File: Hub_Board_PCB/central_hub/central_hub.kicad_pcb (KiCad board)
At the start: 2 copper layers, 0.6 x 1.7 mm, 90 parts, among them J1 CAN_OUT, J10 Conn_02x03_Counter_Clockwise, J2 Barrel_Jack_MountingPin, J3 Screw_Terminal_01x14, J4 Conn_02x05_Counter_Clockwise, J5 CSP-USC16-TR, J6 Screw_Terminal_01x08, J7 Conn_02x03_Counter_Clockwise, J8 Conn_01x02, J9 Screw_Terminal_01x04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

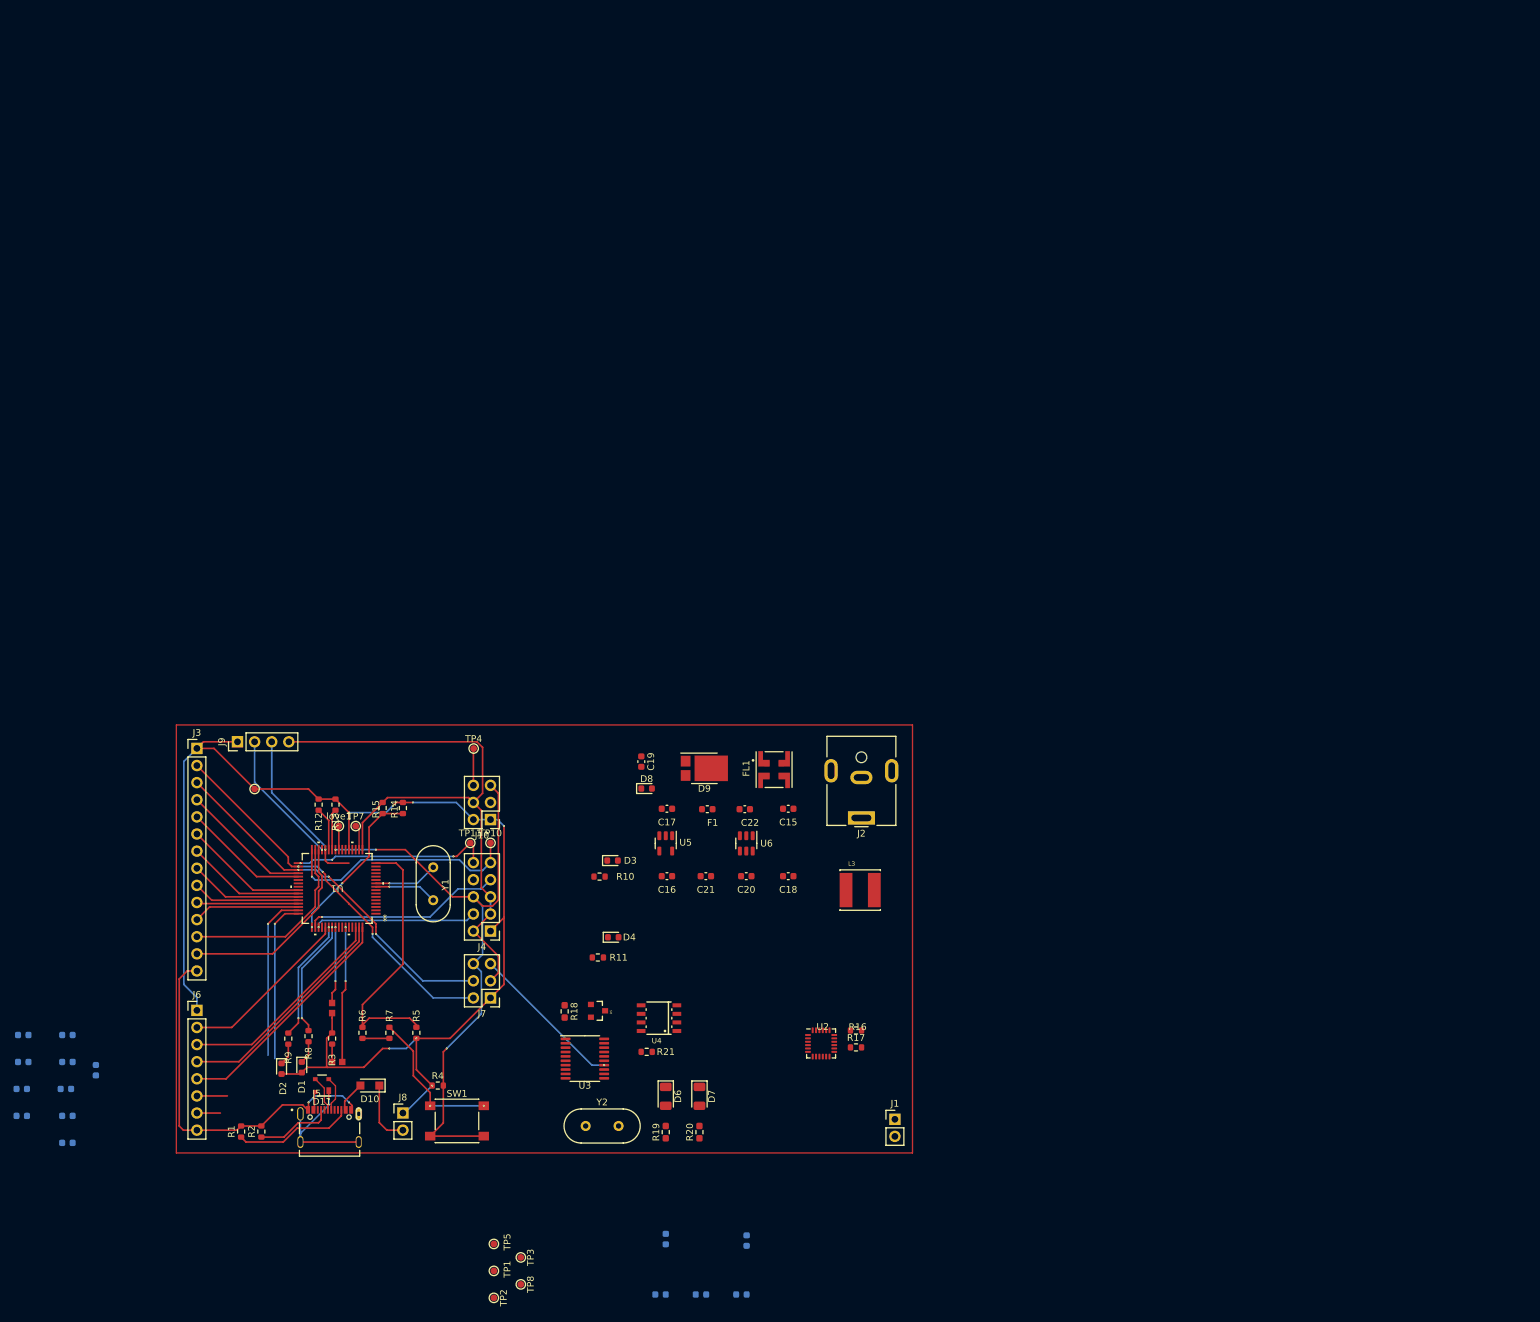
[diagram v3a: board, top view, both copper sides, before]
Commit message: Added new connectors as per brandons new shifters
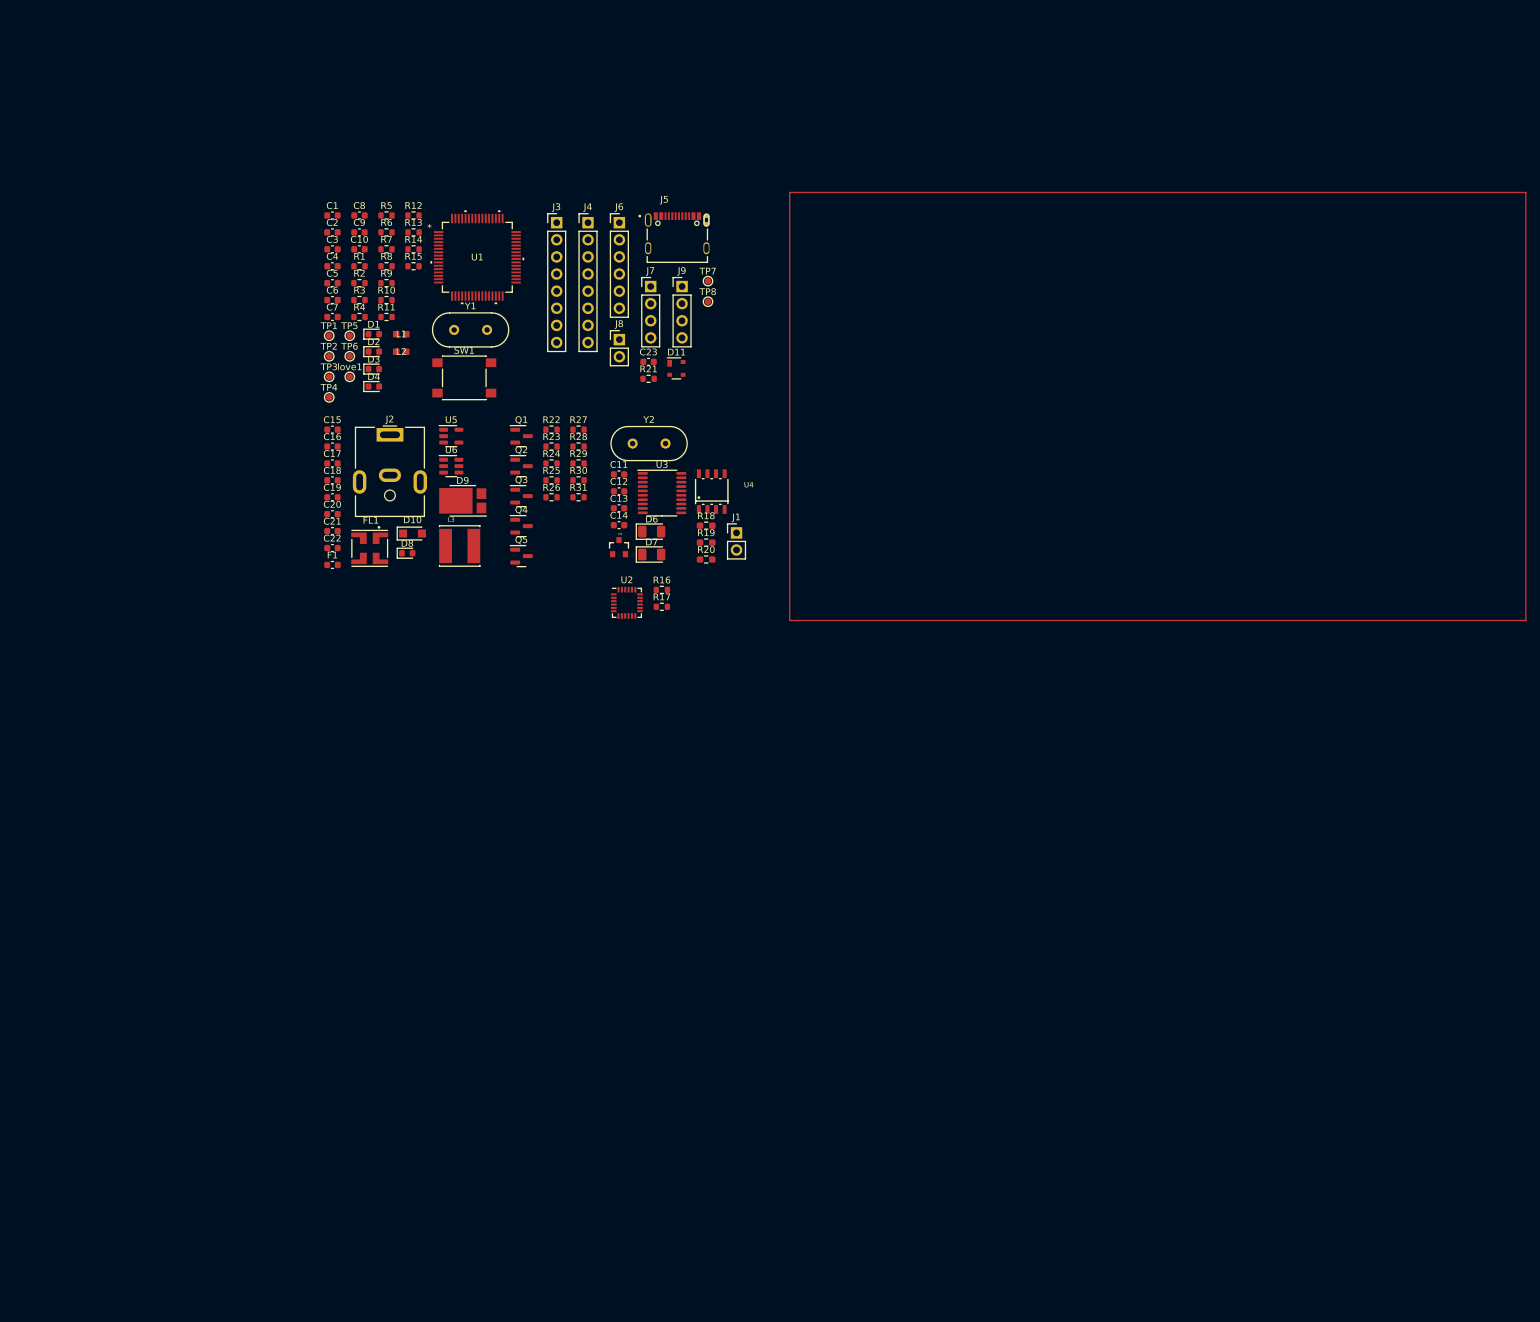
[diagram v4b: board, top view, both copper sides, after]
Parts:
- removed J10: Conn_02x03_Counter_Clockwise, Connector_PinHeader_2.54mm:PinHeader_2x03_P2.54mm_Vertical
- removed TP10, TP11: TestPoint, TestPoint:TestPoint_Pad_D1.0mm
- added Q1: BSS138, Package_TO_SOT_SMD:SOT-23, F.Cu at (139.6, 31.6)
- added Q2: BSS138, Package_TO_SOT_SMD:SOT-23, F.Cu at (139.6, 36.1)
- added Q3: BSS138, Package_TO_SOT_SMD:SOT-23, F.Cu at (139.6, 40.5)
- added Q4: BSS138, Package_TO_SOT_SMD:SOT-23, F.Cu at (139.6, 45.0)
- added Q5: BSS138, Package_TO_SOT_SMD:SOT-23, F.Cu at (139.6, 49.5)
- added R22: 10k, Resistor_SMD:R_0603_1608Metric, F.Cu at (144.1, 30.7)
- added R23: 10k, Resistor_SMD:R_0603_1608Metric, F.Cu at (144.1, 33.2)
- added R24: 10k, Resistor_SMD:R_0603_1608Metric, F.Cu at (144.1, 35.7)
- added R25: 10k, Resistor_SMD:R_0603_1608Metric, F.Cu at (144.1, 38.2)
- added R26: 10k, Resistor_SMD:R_0603_1608Metric, F.Cu at (144.1, 40.7)
- added R27: 10k, Resistor_SMD:R_0603_1608Metric, F.Cu at (148.1, 30.7)
- added R28: 10k, Resistor_SMD:R_0603_1608Metric, F.Cu at (148.1, 33.2)
- added R29: 10k, Resistor_SMD:R_0603_1608Metric, F.Cu at (148.1, 35.7)
- added R30: 10k, Resistor_SMD:R_0603_1608Metric, F.Cu at (148.1, 38.2)
- added R31: 10k, Resistor_SMD:R_0603_1608Metric, F.Cu at (148.1, 40.7)
- C1, C10, C11, C12, C13, C14, C2, C23, C3, C4, C5, C6, C7, C8, C9: moved to F.Cu
- J3: value Screw_Terminal_01x14 -> Screw_Terminal_01x08; footprint Connector_PinHeader_2.54mm:PinHeader_1x14_P2.54mm_Vertical -> Connector_PinHeader_2.54mm:PinHeader_1x08_P2.54mm_Vertical
- J4: value Conn_02x05_Counter_Clockwise -> Screw_Terminal_01x08; footprint Connector_PinHeader_2.54mm:PinHeader_2x05_P2.54mm_Vertical -> Connector_PinHeader_2.54mm:PinHeader_1x08_P2.54mm_Vertical
- J6: value Screw_Terminal_01x08 -> Screw_Terminal_01x06; footprint Connector_PinHeader_2.54mm:PinHeader_1x08_P2.54mm_Vertical -> Connector_PinHeader_2.54mm:PinHeader_1x06_P2.54mm_Vertical
- J7: value Conn_02x03_Counter_Clockwise -> Screw_Terminal_01x04; footprint Connector_PinHeader_2.54mm:PinHeader_2x03_P2.54mm_Vertical -> Connector_PinHeader_2.54mm:PinHeader_1x04_P2.54mm_Vertical
- R16, R17: value 5.1k -> 4.7k
- moved TP8 148.4 mm to (167.3, 11.7), turned to 0 degrees
- moved C1 143.1 mm to (111.5, -1.09), turned to 0 degrees
- moved J5 142.3 mm to (162.7, -1.00)
- moved TP2 141.8 mm to (111.1, 19.8), turned to 0 degrees
- moved TP1 140.9 mm to (111.1, 16.8), turned to 0 degrees
- moved C9 140.3 mm to (115.6, 1.42), turned to 0 degrees
- moved TP5 136.4 mm to (114.1, 16.8), turned to 0 degrees
- moved TP3 133.7 mm to (111.1, 22.9), turned to 0 degrees
- moved C8 132.9 mm to (115.6, -1.09), turned to 0 degrees
- moved C3 132.8 mm to (111.5, 3.93), turned to 0 degrees
- moved J6 132.6 mm to (154.1, -0.02)
- moved C2 131.4 mm to (111.5, 1.42), turned to 0 degrees
- moved C23 130.2 mm to (158.4, 20.6), turned to 0 degrees
- moved C5 129.7 mm to (111.5, 8.95), turned to 0 degrees
- moved R1 129.6 mm to (115.6, 6.44), turned to 0 degrees
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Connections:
- C12 pad 1: IOREF -> +5V
- C14 pad 1: IOREF -> +5V
- C16 pad 2: IOREF -> +5V
- C20 pad 2: IOREF -> +5V
- C21 pad 2: IOREF -> +5V
- C4 pad 2: IOREF -> +5V
- C5 pad 2: IOREF -> +5V
- C6 pad 2: IOREF -> +5V
- D1 pad 2: IOREF -> +5V
- D2 pad 2: IOREF -> +5V
- D3 pad 2: IOREF -> +5V
- J3 pad 1: IOREF -> +5V
- J3 pad 2: D11 -> D7
- J3 pad 3: D12 -> D6
- J3 pad 4: D13 -> D2
- J3 pad 5: D10 -> D3
- J3 pad 6: D7 -> D0
- J3 pad 7: D6 -> D1
- J3 pad 8: D2 -> GND
- J4 pad 1: IOREF -> +5V
- J4 pad 3: GND -> D10_3.3V
- J4 pad 4: P502 -> D4_3.3V
- J4 pad 5: GND -> D5_3.3V
- J4 pad 6: ~{RESET} -> D11_3.3V
- J4 pad 7: P501 -> D13_3.3V
- J4 pad 8: unconnected-(J4-Pin_8-Pad8) -> +3.3V
- J6 pad 1: IOREF -> A0
- J6 pad 2: A0 -> A3
- J6 pad 3: A3 -> A2
- J6 pad 4: A2 -> A1
- J6 pad 5: A1 -> A4
- J6 pad 6: A4 -> A5
- J7 pad 2: D11 -> BOOT
- J7 pad 3: GND -> ~{RESET}
- J7 pad 4: D12 -> GND
- J8 pad 1: IOREF -> +5V
- J9 pad 1: IOREF -> +5V
- L2 pad 2: IOREF -> +5V
- L3 pad 2: IOREF -> +5V
- R12 pad 1: IOREF -> +5V
- R13 pad 1: IOREF -> +5V
- R14 pad 1: IOREF -> +5V
- R19 pad 1: IOREF -> +5V
- R20 pad 1: IOREF -> +5V
- R3 pad 1: IOREF -> +5V
- R4 pad 1: IOREF -> +5V
- R5 pad 1: IOREF -> +5V
- TP3 pad 1: IOREF -> +5V
- TP6 pad 1: IOREF -> +5V
- U1 pad 11: IOREF -> +5V
- U1 pad 21: IOREF -> +5V
- U1 pad 39: IOREF -> +5V
- U3 pad 20: IOREF -> +5V
- U4 pad 3: IOREF -> +5V
- U5 pad 1: IOREF -> +5V
- U5 pad 3: IOREF -> +5V
- U6 pad 1: IOREF -> +5V
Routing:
- net IOREF: track 191.2 -> 0.00 mm, vias 7 -> 0
- net GND: track 168.1 -> 0.00 mm, vias 4 -> 0
- net ~{RESET}: track 93.7 -> 0.00 mm, vias 3 -> 0
- net D11: track 57.2 -> 0.00 mm, vias 3 -> 0
- net D12: track 54.1 -> 0.00 mm, vias 3 -> 0
- net D13: track 42.7 -> 0.00 mm, vias 1 -> 0
- net Net-(U1-P407/USB_VBUS/ADTRG0): track 39.8 -> 0.00 mm
- net P300: track 36.0 -> 0.00 mm, vias 1 -> 0
- net A1: track 35.2 -> 0.00 mm
- net A2: track 33.6 -> 0.00 mm
- net A3: track 31.9 -> 0.00 mm
- net P108: track 30.1 -> 0.00 mm, vias 3 -> 0
- net D1: track 29.9 -> 0.00 mm
- net P501: track 29.5 -> 0.00 mm, vias 1 -> 0
- net A4: track 29.3 -> 0.00 mm, vias 1 -> 0
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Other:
- board size 0.6 x 1.7 mm -> 0.7 x 1.7 mm

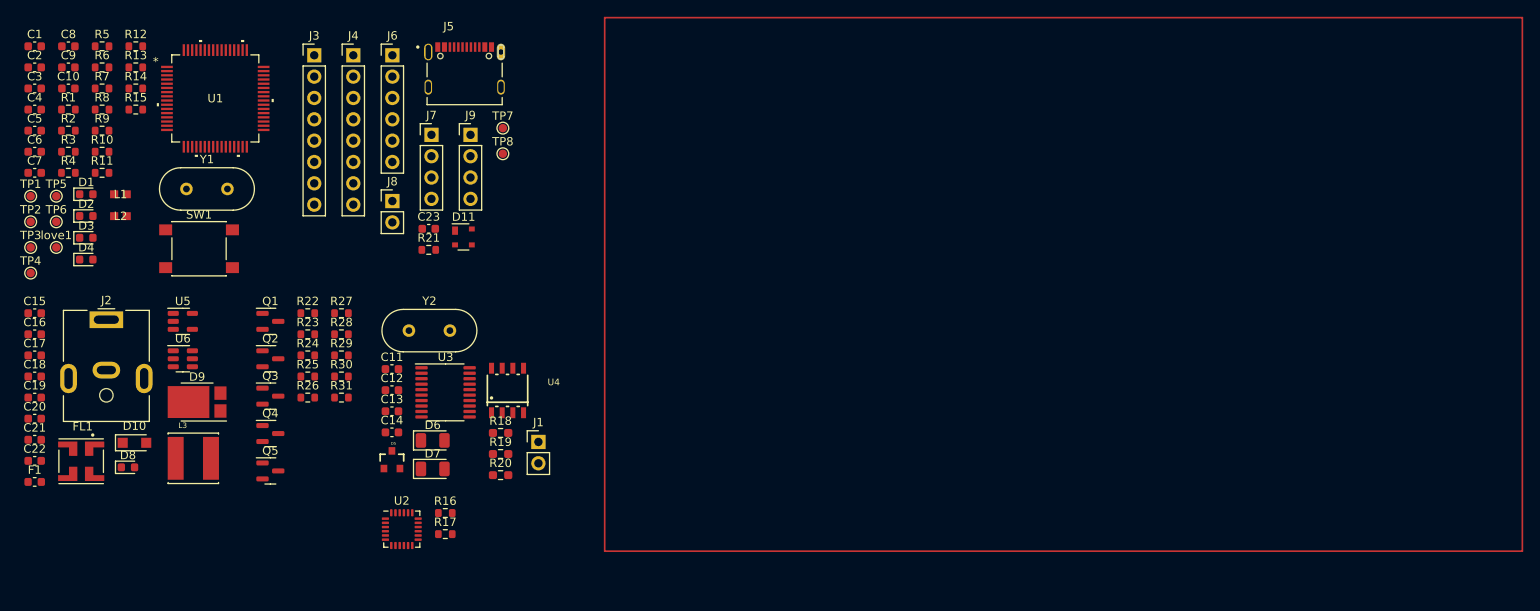
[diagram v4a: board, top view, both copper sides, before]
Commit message: Prelim layout + routing for hub PCB
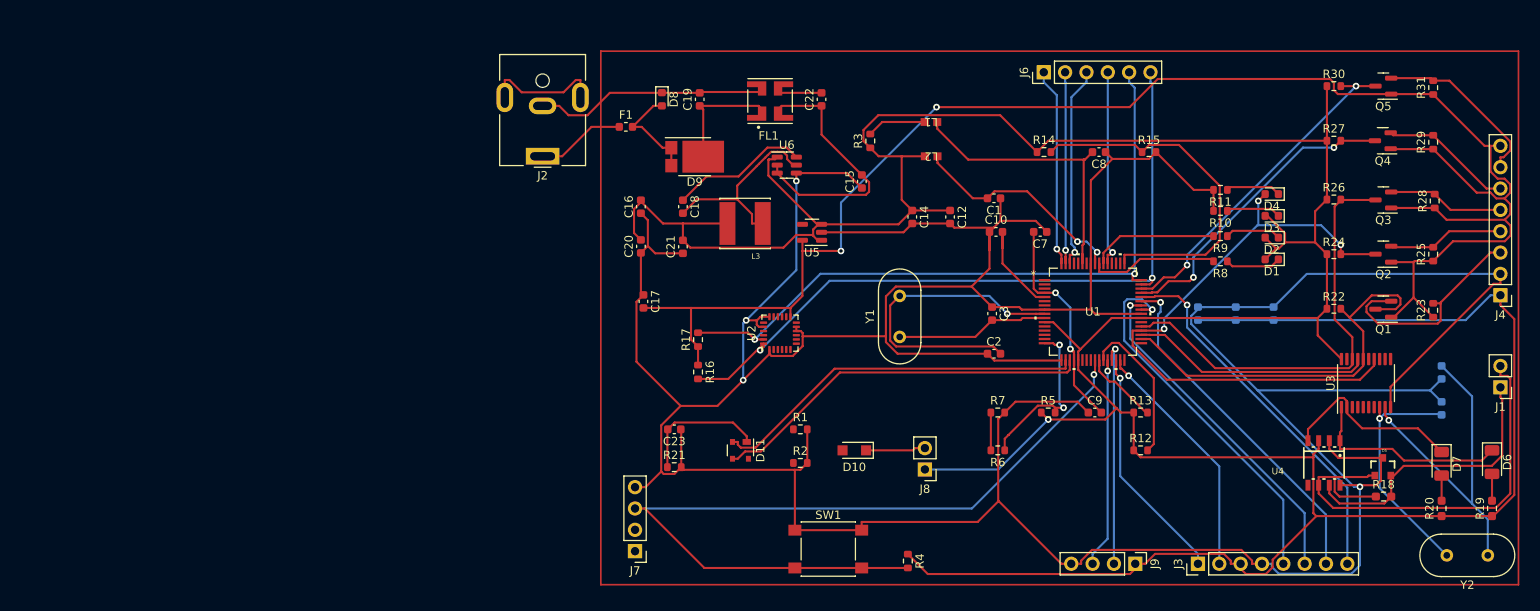
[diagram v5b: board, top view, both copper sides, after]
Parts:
- removed J5: CSP-USC16-TR, ~ALL:VALCON_CSP-USC16-TR
- removed TP1, TP2, TP3, TP4, TP5, TP6, TP7, TP8, love1: TestPoint, TestPoint:TestPoint_Pad_D1.0mm
- C11, C13, C4, C5, C6: moved to B.Cu
- moved C6 148.7 mm to (259.0, 30.7), turned to -90 degrees
- moved C5 144.6 mm to (254.5, 30.7), turned to -90 degrees
- moved D4 141.3 mm to (258.8, 16.5), turned to 180 degrees
- moved D1 141.3 mm to (258.8, 24.3), turned to 180 degrees
- moved D3 141.1 mm to (258.8, 19.1), turned to 180 degrees
- moved D2 141.1 mm to (258.8, 21.7), turned to 180 degrees
- moved C4 140.6 mm to (250.0, 30.7), turned to -90 degrees
- moved Q5 140.2 mm to (272.1, 3.65), turned to 180 degrees
- moved J4 139.5 mm to (286.0, 28.5), turned to 180 degrees
- moved Q4 136.9 mm to (272.0, 10.2), turned to 180 degrees
- moved R31 135.1 mm to (278.0, 3.83), turned to 90 degrees
- moved R25 134.7 mm to (278.0, 23.6), turned to 90 degrees
- moved Q3 134.5 mm to (272.1, 17.2), turned to 180 degrees
- moved R8 134.3 mm to (252.7, 24.5), turned to 180 degrees
- moved R23 134.0 mm to (278.0, 30.3), turned to 90 degrees
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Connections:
- J3 pad 1: +5V -> D1
- J3 pad 2: D7 -> D0
- J3 pad 3: D6 -> +5V
- J3 pad 4: D2 -> GND
- J3 pad 5: D3 -> D7
- J3 pad 6: D0 -> D6
- J3 pad 7: D1 -> D2
- J3 pad 8: GND -> D3
- J4 pad 3: D10_3.3V -> D11_3.3V
- J4 pad 4: D4_3.3V -> D13_3.3V
- J4 pad 5: D5_3.3V -> D10_3.3V
- J4 pad 6: D11_3.3V -> D4_3.3V
- J4 pad 7: D13_3.3V -> D5_3.3V
- J6 pad 1: A0 -> A1
- J6 pad 2: A3 -> A2
- J6 pad 3: A2 -> A3
- J6 pad 4: A1 -> A0
- J6 pad 5: A4 -> A5
- J6 pad 6: A5 -> A4
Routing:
- net GND: track 0.00 -> 525.5 mm, vias 0 -> 4
- net +5V: track 0.00 -> 440.9 mm, vias 0 -> 1
- net +3.3V: track 0.00 -> 203.1 mm, vias 0 -> 2
- net ~{RESET}: track 0.00 -> 100.0 mm, vias 0 -> 1
- net A4: track 0.00 -> 87.2 mm, vias 0 -> 2
- net A5: track 0.00 -> 82.7 mm, vias 0 -> 2
- net D13: track 0.00 -> 74.6 mm, vias 0 -> 3
- net /CAN/CAN_LOW: track 0.00 -> 56.0 mm
- net D10: track 0.00 -> 52.7 mm
- net D11: track 0.00 -> 47.9 mm
- net USB_D+: track 0.00 -> 46.3 mm
- net USB_D-: track 0.00 -> 45.5 mm
- net D3: track 0.00 -> 44.6 mm, vias 0 -> 1
- net D7: track 0.00 -> 44.3 mm, vias 0 -> 1
- net Net-(U1-GTIOC2A/AN016/P500): track 0.00 -> 42.8 mm
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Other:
- board outline removed
